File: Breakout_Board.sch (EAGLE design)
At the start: 89 parts, among them IC101 AD8620R, IC102 AD8620R, IC103 ADE7880, IC104 RH/H6, IC105 7805TV, Q101 16M384, U101 ADR512ARTZ-REEL7, U102 SI8640BD-B-IS, U103 SI8641BD-B-IS, X1 231-538/001-000, X101 STL266-04, X103 MKDSN1,5/2-5,08

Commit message: Board layout updated
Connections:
- net IAN: now also C2.2, R1.2, R3.2, X1.P2; no longer C109.2, R106.1, R112.2, X1.P8
- net IAP: now also C2.1, R2.2; no longer C109.1, R127.2
- net IBN: now also C107.2, R104.2, R110.2, X1.P3; no longer C108.2, R105.1, R111.2, X1.P6
- net IBP: now also C107.1, R125.2; no longer C108.1, R126.2
- net ICN: now also C108.2, R105.2, R111.2, X1.P6; no longer C107.2, R104.1, R110.2, X1.P4
- net ICP: now also C108.1, R126.2; no longer C107.1, R125.2
- net INN: now also C109.2, R106.1, R112.2, X1.P7; no longer C2.2, R1.1, R3.2, X1.P2
- net INP: now also C109.1, R127.2; no longer C2.1, R2.2
- net IN_I1: now also IC102A.IN+, R104.1, X1.P4; no longer IC101A.IN+, R104.2, X1.P3
- net IN_I2: now also R105.1; no longer R105.2
- net IN_I3: now also IC101A.IN+, X1.P8; no longer IC102A.IN+, X1.P7
- net N$18: now also IC101A.OUT; no longer IC102A.OUT
- net N$19: now also IC102A.IN-; no longer IC101A.IN-
- net N$21: now also IC102A.OUT; no longer IC101A.OUT
- net N$23: now also R1.1; no longer R1.2
- net N$29: now also IC101A.IN-; no longer IC102A.IN-
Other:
- moved on the sheet: IC101A, IC102A, R1, R104, R105

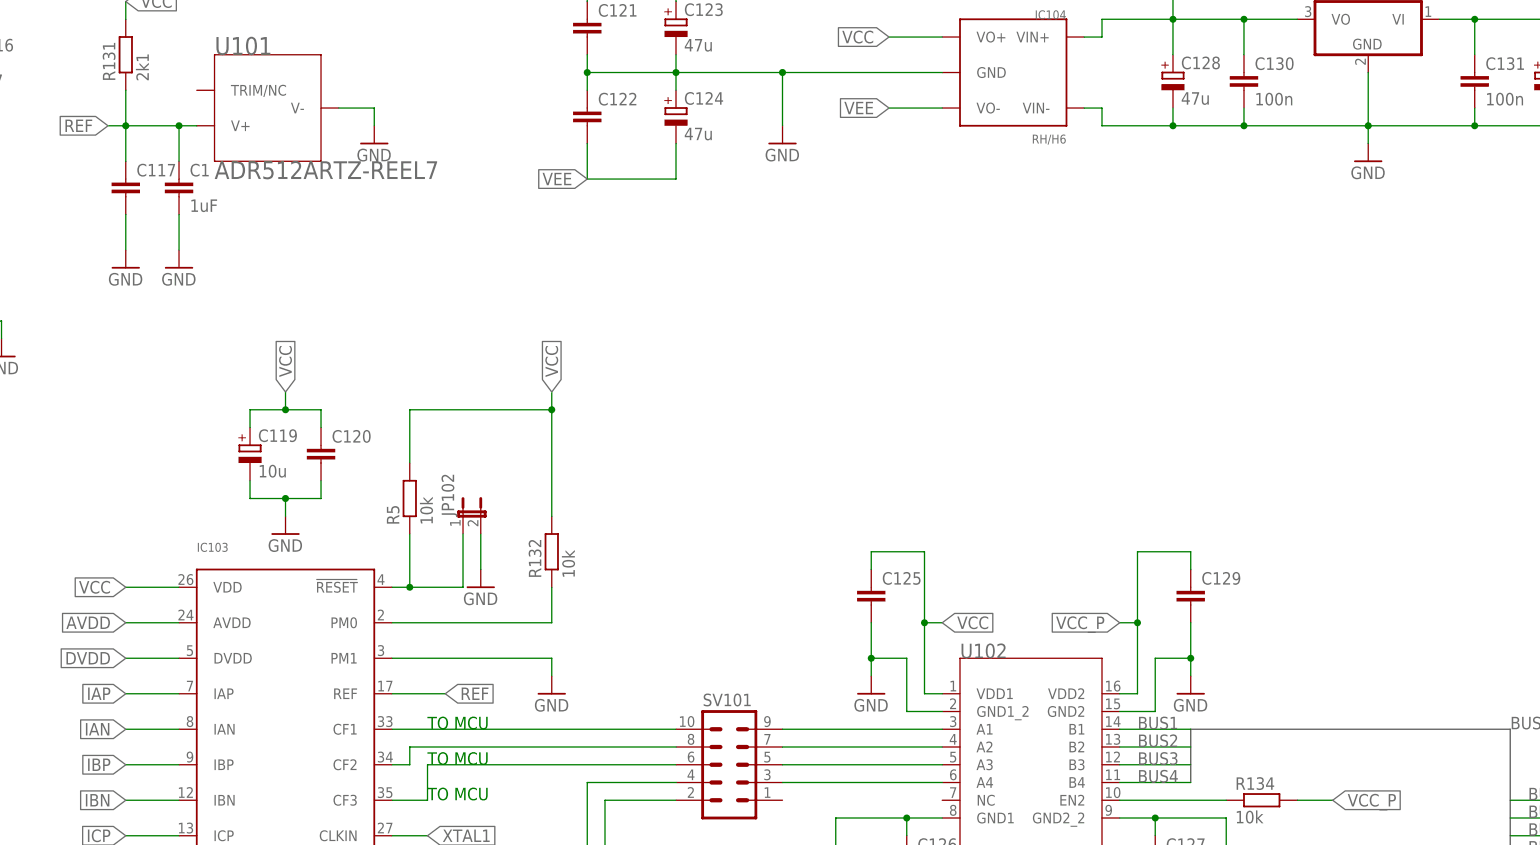
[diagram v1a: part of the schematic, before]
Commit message: Board layout finished without checking DRC
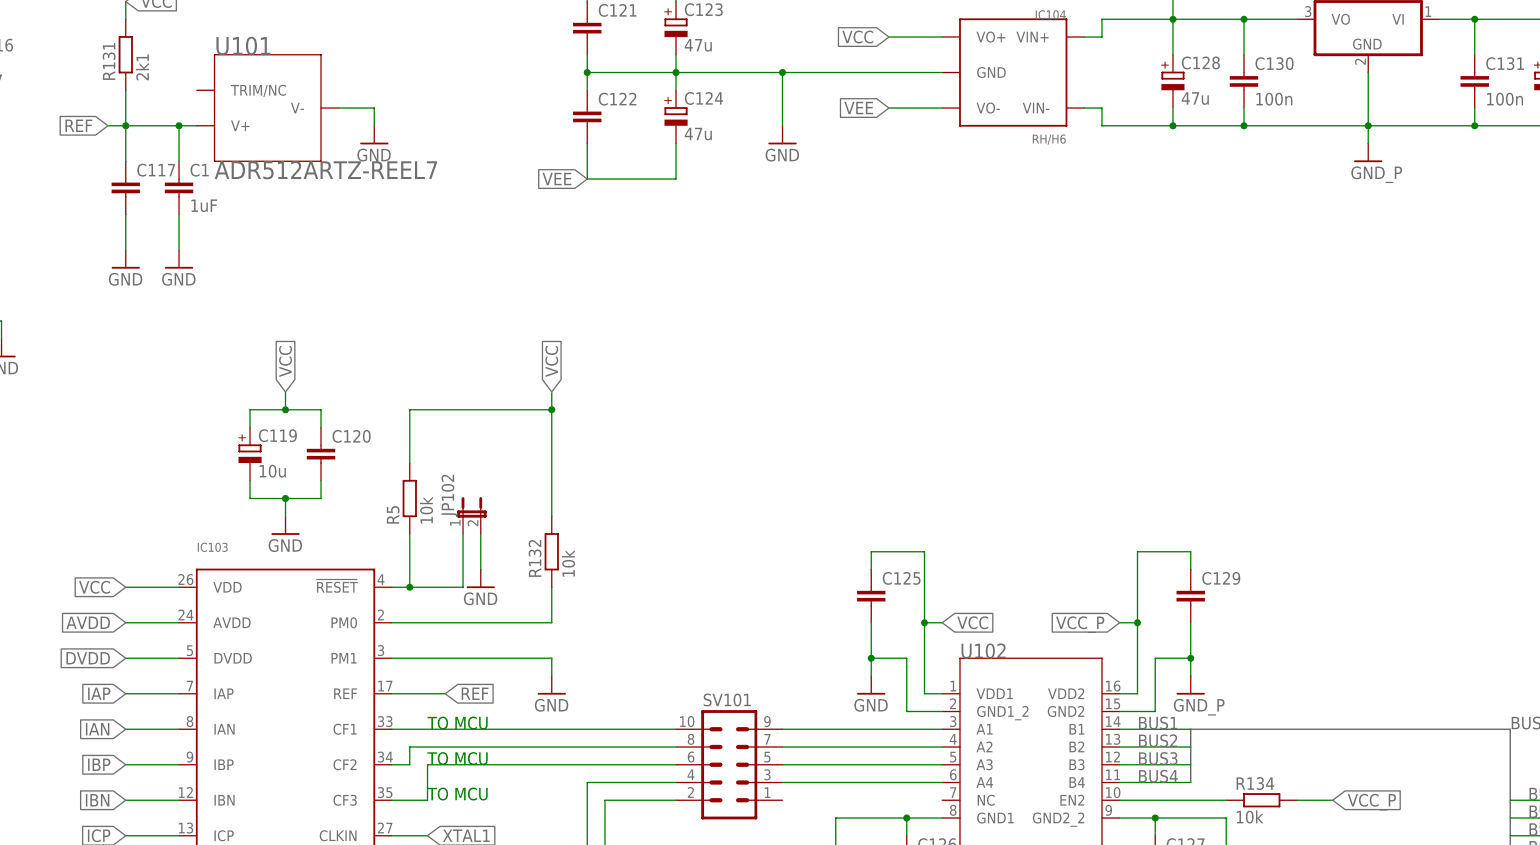
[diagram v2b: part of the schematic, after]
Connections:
- net GND: now also C117.2
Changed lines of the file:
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@@
 <part name="C127" library="rcl" deviceset="C-EU" device="C0603K" value="100n"/>
 <part name="GND115" library="supply1" deviceset="GND" device=""/>
-<part name="GND116" library="supply1" deviceset="GND" device=""/>
+<part name="GND116" library="supply1" deviceset="GND" device="" value="GND_P"/>
 <part name="GND114" library="supply1" deviceset="GND" device=""/>
 <part name="GND113" library="supply1" deviceset="GND" device=""/>
@@
 <part name="C131" library="rcl" deviceset="C-EU" device="C0603K" value="100n"/>
 <part name="C132" library="rcl" deviceset="CPOL-EU" device="D" value="47u"/>
-<part name="GND119" library="supply1" deviceset="GND" device=""/>
+<part name="GND119" library="supply1" deviceset="GND" device="" value="GND_P"/>
 <part name="SV102" library="con-lstb" deviceset="MA08-1" device=""/>
 <part name="X103" library="con-phoenix-508" deviceset="MKDSN1,5/2-5,08" device=""/>
@@
 </segment>
 </net>
-<net name="ICP" class="2">
+<net name="ICP" class="0">
 <segment>
 <pinref part="IC103" gate="G$1" pin="ICP"/>
@@
 </segment>
 <segment>
-<wire x1="165.1" y1="226.06" x2="165.1" y2="220.98" width="0.1524" layer="91"/>
-<pinref part="GND103" gate="1" pin="GND"/>
-</segment>
-<segment>
 <wire x1="172.72" y1="226.06" x2="172.72" y2="220.98" width="0.1524" layer="91"/>
 <pinref part="GND105" gate="1" pin="GND"/>
@@
 </segment>
 <segment>
-<pinref part="GND119" gate="1" pin="GND"/>
-<wire x1="342.9" y1="236.22" x2="342.9" y2="238.76" width="0.1524" layer="91"/>
-</segment>
-<segment>
 <pinref part="IC103" gate="G$1" pin="AGND"/>
 <wire x1="172.72" y1="96.52" x2="167.64" y2="96.52" width="0.1524" layer="91"/>
@@
 <wire x1="147.32" y1="210.82" x2="139.7" y2="210.82" width="0.1524" layer="91"/>
 <junction x="139.7" y="210.82"/>
+</segment>
+<segment>
+<pinref part="GND103" gate="1" pin="GND"/>
+<pinref part="C117" gate="G$1" pin="2"/>
+<wire x1="165.1" y1="220.98" x2="165.1" y2="226.06" width="0.1524" layer="91"/>
 </segment>
 </net>
@@
 <wire x1="378.46" y1="238.76" x2="368.3" y2="238.76" width="0.1524" layer="91"/>
 <junction x="368.3" y="238.76"/>
+<pinref part="GND119" gate="1" pin="GND"/>
+<wire x1="342.9" y1="238.76" x2="342.9" y2="236.22" width="0.1524" layer="91"/>
 </segment>
 </net>
@@
 </sheet>
 </sheets>
+<errors>
+</errors>
 </schematic>
 </drawing>

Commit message: First official release!
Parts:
- R1, R104, R105, R106: value 0R01 -> 4R7
- R110, R111, R112, R3: value 150R -> 6k49
- R119, R120, R121, R4: value 221k -> 2k21
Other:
- note added: "Dimensioniert auf 25 A Verstärkungsfaktor 1+ 0,3251"
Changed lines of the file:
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@@
 </class>
 <class number="1" name="HighU" width="0" drill="0">
-<clearance class="0" value="2"/>
+<clearance class="0" value="0.0254"/>
 </class>
 <class number="2" name="HIghI" width="0" drill="0">
-<clearance class="0" value="2"/>
+<clearance class="0" value="0.0254"/>
 <clearance class="1" value="2"/>
 </class>
@@
 <part name="R130" library="rcl" deviceset="R-EU_" device="R0603" value="1k"/>
 <part name="C112" library="rcl" deviceset="C-EU" device="C0603K" value="2n2"/>
-<part name="R104" library="rcl" deviceset="R-EU_" device="R0603" value="0R01"/>
+<part name="R104" library="rcl" deviceset="R-EU_" device="R0603" value="4R7"/>
 <part name="IC101" library="analog-devices" deviceset="AD8620" device="R"/>
 <part name="IC102" library="analog-devices" deviceset="AD8620" device="R"/>
 <part name="R125" library="rcl" deviceset="R-EU_" device="R0603" value="1k"/>
 <part name="C107" library="rcl" deviceset="C-EU" device="C0603K" value="2n2"/>
-<part name="R110" library="rcl" deviceset="R-EU_" device="R0603" value="150R"/>
-<part name="R119" library="rcl" deviceset="R-EU_" device="R0603" value="221k"/>
-<part name="R105" library="rcl" deviceset="R-EU_" device="R0603" value="0R01"/>
+<part name="R110" library="rcl" deviceset="R-EU_" device="R0603" value="6k49"/>
+<part name="R119" library="rcl" deviceset="R-EU_" device="R0603" value="2k21"/>
+<part name="R105" library="rcl" deviceset="R-EU_" device="R0603" value="4R7"/>
 <part name="R126" library="rcl" deviceset="R-EU_" device="R0603" value="1k"/>
 <part name="C108" library="rcl" deviceset="C-EU" device="C0603K" value="2n2"/>
-<part name="R111" library="rcl" deviceset="R-EU_" device="R0603" value="150R"/>
-<part name="R120" library="rcl" deviceset="R-EU_" device="R0603" value="221k"/>
-<part name="R106" library="rcl" deviceset="R-EU_" device="R0603" value="0R01"/>
+<part name="R111" library="rcl" deviceset="R-EU_" device="R0603" value="6k49"/>
+<part name="R120" library="rcl" deviceset="R-EU_" device="R0603" value="2k21"/>
+<part name="R106" library="rcl" deviceset="R-EU_" device="R0603" value="4R7"/>
 <part name="R127" library="rcl" deviceset="R-EU_" device="R0603" value="1k"/>
 <part name="C109" library="rcl" deviceset="C-EU" device="C0603K" value="2n2"/>
-<part name="R112" library="rcl" deviceset="R-EU_" device="R0603" value="150R"/>
-<part name="R121" library="rcl" deviceset="R-EU_" device="R0603" value="221k"/>
+<part name="R112" library="rcl" deviceset="R-EU_" device="R0603" value="6k49"/>
+<part name="R121" library="rcl" deviceset="R-EU_" device="R0603" value="2k21"/>
 <part name="IC104" library="recom_own" deviceset="RH/H6" device=""/>
 <part name="R132" library="rcl" deviceset="R-EU_" device="R0603" value="10k"/>
@@
 <part name="GND107" library="supply1" deviceset="GND" device=""/>
 <part name="C1" library="rcl" deviceset="C-EU" device="C0603K" value="1uF"/>
-<part name="R1" library="rcl" deviceset="R-EU_" device="R0603" value="0R01"/>
+<part name="R1" library="rcl" deviceset="R-EU_" device="R0603" value="4R7"/>
 <part name="R2" library="rcl" deviceset="R-EU_" device="R0603" value="1k"/>
 <part name="C2" library="rcl" deviceset="C-EU" device="C0603K" value="2n2"/>
-<part name="R3" library="rcl" deviceset="R-EU_" device="R0603" value="150R"/>
-<part name="R4" library="rcl" deviceset="R-EU_" device="R0603" value="221k"/>
+<part name="R3" library="rcl" deviceset="R-EU_" device="R0603" value="6k49"/>
+<part name="R4" library="rcl" deviceset="R-EU_" device="R0603" value="2k21"/>
 <part name="X1" library="con-wago_5.08mm" deviceset="231-538/001-000" device=""/>
 <part name="R5" library="rcl" deviceset="R-EU_" device="R0603" value="10k"/>
@@
 <text x="43.18" y="220.98" size="1.778" layer="91">29pF = 2x18pF (C_L) - 7pF (C_P)</text>
 <text x="60.96" y="218.44" size="1.778" layer="91">30pF should fit</text>
+<text x="30.48" y="198.12" size="1.778" layer="91">Dimensioniert auf 25 A
+Verstärkungsfaktor 1+ 0,3251</text>
 </plain>
 <instances>
@@
 </schematic>
 </drawing>
+<compatibility>
+<note version="6.3" minversion="6.2.2" severity="warning">
+Since Version 6.2.2 text objects can contain more than one line,
+which will not be processed correctly with this version.
+</note>
+</compatibility>
 </eagle>

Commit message: A1 schematic and layout
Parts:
- removed C102, C103, C105, C106: 220n, rcl:C-EUC0603K
- removed C107, C108, C109: 2n2, rcl:C-EUC0603K
- removed C122: (no value), rcl:C-EUC0603K
- removed C124: 47u, rcl:CPOL-EUD
- removed IC101, IC102: AD8620R, analog-devices:AD8620R
- removed IC104: RH/H6, recom_own:RH/H6
- removed R104, R105, R106: 4R7, rcl:R-EU_R0603
- removed R110, R111, R112: 6k49, rcl:R-EU_R0603
- removed R119, R120, R121: 2k21, rcl:R-EU_R0603
- removed R125, R126, R127: 1k, rcl:R-EU_R0603
- added C3, C4, C5, C6, C7, C8, C9: 2n2, rcl:C-EUC0603K
- added IC1: RH-0505S/H6, recom_own:RH-0505S/H6
- added R10, R11, R14, R15, R18, R6, R7: 2R7, rcl:R-EU_R0805
- added R12, R13, R16, R17, R8, R9: 150R, rcl:R-EU_R0805
- added R19, R20, R21, R22, R23, R24, R25: 1k, rcl:R-EU_R0603
- R1: value 4R7 -> 2R7; device rcl:R-EU_R0603 -> rcl:R-EU_R0805
- R3: value 6k49 -> 150R; device rcl:R-EU_R0603 -> rcl:R-EU_R0805
- R4: value 2k21 -> 150R; device rcl:R-EU_R0603 -> rcl:R-EU_R0805
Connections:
- removed net AGND: C113.2, C114.-
- removed net DGND: C115.2, C116.-
- removed net IN_I1: IC102A.IN+, R104.1, X1.P4
- removed net IN_I2: IC101B.IN+, R105.1, X1.P5
- removed net IN_I3: IC101A.IN+, R106.2, X1.P8
- removed net N$16: IC101B.OUT, R120.1, R126.1
- removed net N$17: IC102B.IN-, R3.1, R4.2
- removed net N$18: IC101A.OUT, R121.1, R127.1
- removed net N$19: IC102A.IN-, R110.1, R119.2
- removed net N$21: IC102A.OUT, R119.1, R125.1
- removed net N$22: IC102B.OUT, R2.1, R4.1
- removed net N$23: IC102B.IN+, R1.1, X1.P1
- removed net N$24: IC101B.IN-, R111.1, R120.2
- removed net N$29: IC101A.IN-, R112.1, R121.2
- removed net VEE: C103.2, C106.2, C122.2, C124.-, IC101P.V-, IC102P.V-, IC104.VO-
- new net INH: R15.2, R16.2, R24.1, X1.P7
- new net INL: R17.1, R18.1, R25.1, X1.P8
- new net L1H: R1.2, R2.1, R3.2, X1.P1
- new net L1L: R19.1, R4.1, R6.1, X1.P2
- new net L2H: R20.1, R7.2, R8.2, X1.P3
- new net L2L: R10.1, R21.1, R9.1, X1.P4
- new net L3H: R11.2, R12.2, R22.1, X1.P5
- new net L3L: R13.1, R14.1, R23.1, X1.P6
- net GND: now also C113.2, C114.-, C115.2, C116.-, C2.2, C3.1, C4.2, C5.1, C6.2, C7.1, C8.2, C9.1, IC1.VOUT-, R1.1, R10.2, R11.1, R12.1, R13.2, R14.2, R15.1, R16.1, R17.2, R18.2, R3.1, R4.2, R6.2, R7.1, R8.1, R9.2; no longer C102.2, C103.1, C105.2, C106.1, C122.1, C124.+, IC104.GND
- net GND_P: now also IC1.VIN-; no longer IC104.VIN-
- net IAN: now also C3.2, R19.2; no longer C2.2, R1.2, R3.2, X1.P2
- net IBN: now also C5.2, R21.2; no longer C107.2, R104.2, R110.2, X1.P3
- net IBP: now also C4.1, R20.2; no longer C107.1, R125.2
- net ICN: now also C7.2, R23.2; no longer C108.2, R105.2, R111.2, X1.P6
- net ICP: now also C6.1, R22.2; no longer C108.1, R126.2
- net INN: now also C9.2, R25.2; no longer C109.2, R106.1, R112.2, X1.P7
- net INP: now also C8.1, R24.2; no longer C109.1, R127.2
- net VCC: now also IC1.VOUT+; no longer C102.1, C105.1, IC101P.V+, IC102P.V+, IC104.VO+
- net VCC_P: now also IC1.VIN+; no longer IC104.VIN+
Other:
- note removed: "29pF = 2x18pF (C_L) - 7pF (C_P)"
- note removed: "30pF should fit"
- note removed: "Dimensioniert auf 25 A Verstärkungsfaktor 1+ 0,3251"
- moved on the sheet: C121, C123, C2, R1, R2, R3, R4, X1

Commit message: -updated sch and brd, added pdf files
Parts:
- removed C1: 1uF, rcl:C-EUC0603K
- removed C132: 47u, rcl:CPOL-EUD
- removed C2, C5: 2n2, rcl:C-EUC0603K
- removed IC105: 7805TV, linear:7805TV
- removed R1, R15, R18, R6, R7: 2R7, rcl:R-EU_R0805
- removed R17, R3, R4, R8, R9: 150R, rcl:R-EU_R0805
- removed R20, R21, R22, R23, R24, R25: 1k, rcl:R-EU_R0603
- removed R5: 10k, rcl:R-EU_R0603
- removed X1: 231-538/001-000, con-wago_5.08mm:231-538/001-000
- added C109: 2n2, rcl:C-EUC0603K
- added C118: 10u, rcl:CPOL-EUB
- added C122, C124: 100n, rcl:C-EUC0603K
- added IC101: ADE7880, AnalogDevices_own:ADE7880
- added R104, R105, R106: 162k, rcl:R-EU_R0805
- added R125, R136: 196k, rcl:R-EU_R0805
- added R137, R138, R139: 1k, rcl:R-EU_R0805
- added R140, R141, R142: 1k, rcl:R-EU_R0603
- added R143: 2k1, rcl:R-EU_R0603
- added R144, R145, R146, R147, R148, R149, R150, R151, R152: 10k, rcl:R-EU_R0603
- added X102: STL266-04, con-riacon:STL266-04
- C101, C104: value 30pF -> 2n2
- C112: value 2n2 -> 220n
- C113: value 220n -> 4u7; device rcl:C-EUC0603K -> rcl:CPOL-EUB
- C114, C116: value 4u7 -> 30pF; device rcl:CPOL-EUB -> rcl:C-EUC0603K
- C117: value (none) -> 4u7; device rcl:C-EUC0603K -> rcl:CPOL-EUB
- C119: value 10u -> 100n; device rcl:CPOL-EUB -> rcl:C-EUC0603K
- C120, C125, C129: value (none) -> 100n
- C121: value (none) -> 1uF
- C127, C131: value 100n -> 47u; device rcl:C-EUC0603K -> rcl:CPOL-EUD
- C128: value 47u -> 100n; device rcl:CPOL-EUD -> rcl:C-EUC0603K
- IC103: value ADE7880 -> 7805TV; device AnalogDevices_own:ADE7880 -> linear:7805TV
- R107, R108, R109: value 162k -> 2R7
- R113, R114: value 196k -> 2R7
- R115, R116, R117, R118: value 196k -> 150R
- R122: value 1k -> 150R
- R123, R124: value 1k -> 196k
- R131: value 2k1 -> 1k
- R132, R133: value 10k -> 1k
- R134, R135: value 10k -> 196k; device rcl:R-EU_R0603 -> rcl:R-EU_R0805
- X101: value STL266-04 -> 231-538/001-000; device con-riacon:STL266-04 -> con-wago_5.08mm:231-538/001-000
- renumbered C3 to C102, C4 to C103, C6 to C105, C7 to C106, C8 to C107, C9 to C108, IC1 to IC102, R10 to R110, R11 to R111, R12 to R119, R13 to R120, R14 to R112, R16 to R121, R19 to R127, R2 to R126
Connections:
- removed net N$42: R133.2, U103.EN2
- new net N$16: R150.2, U103.EN2
- net !SS: now also IC101.!SS, R149.1; no longer IC103.!SS
- net AVDD: now also C112.1, C113.+, IC101.AVDD; no longer C113.1, C114.+, IC103.AVDD
- net DVDD: now also C117.+, IC101.DVDD; no longer C116.+, IC103.DVDD
- net GND: now also C112.2, C113.-, C114.2, C116.1, C117.-, C118.-, C119.2, C122.2, C124.2, C125.1, IC101.AGND, IC101.DGND, IC101.PM1, R107.1, R108.2, R109.1, R113.1, R114.2, R115.1, R116.2, R117.1, R118.2, R122.2; no longer C1.2, C113.2, C114.-, C116.-, C117.2, C119.-, C125.2, C126.1, C2.2, C5.1, IC103.AGND, IC103.DGND, IC103.PM1, R1.1, R15.1, R17.2, R18.2, R3.1, R4.2, R6.2, R7.1, R8.1, R9.2
- net GND_P: now also C126.1, C127.-, C128.2, C131.-, IC103.GND; no longer C127.1, C128.-, C131.2, C132.-, IC105.GND
- net IAN: now also IC101.IAN; no longer IC103.IAN
- net IAP: now also C101.1, IC101.IAP; no longer C2.1, IC103.IAP
- net IBN: now also C104.2, IC101.IBN, R129.2; no longer C5.2, IC103.IBN, R21.2
- net IBP: now also IC101.IBP, R128.2; no longer IC103.IBP, R20.2
- net ICN: now also IC101.ICN, R131.2; no longer IC103.ICN, R23.2
- net ICP: now also IC101.ICP, R130.2; no longer IC103.ICP, R22.2
- net INH: now also R113.2, R132.1, X101.P7; no longer R15.2, R24.1, X1.P7
- net INL: now also R114.1, R122.1, R133.1, X101.P8; no longer R17.1, R18.1, R25.1, X1.P8
- net INN: now also IC101.INN, R133.2; no longer IC103.INN, R25.2
- net INP: now also IC101.INP, R132.2; no longer IC103.INP, R24.2
- net L1H: now also R107.2, R115.2, X101.P1; no longer R1.2, R3.2, X1.P1
- net L1L: now also R108.1, R116.1, X101.P2; no longer R4.1, R6.1, X1.P2
- net L2H: now also R109.2, R117.2, R128.1, X101.P3; no longer R20.1, R7.2, R8.2, X1.P3
- net L2L: now also R118.1, R129.1, X101.P4; no longer R21.1, R9.1, X1.P4
- net L3H: now also R130.1, X101.P5; no longer R22.1, X1.P5
- net L3L: now also R131.1, X101.P6; no longer R23.1, X1.P6
- net MISO: now also IC101.MISO, R147.1; no longer IC103.MISO
- net MOSI: now also IC101.MOSI, R148.1; no longer IC103.MOSI
- net N$1: now also R104.1; no longer R107.1
- net N$10: now also X102.3; no longer X101.3
- net N$11: now also R106.1; no longer R109.1
- net N$12: now also R106.2, R125.1; no longer R109.2, R115.1
- net N$13: now also R125.2, R136.1; no longer R115.2, R118.1
- net N$14: now also R136.2, R139.2, R142.1; no longer R118.2, R124.2, R130.1
- net N$15: now also X102.2; no longer X101.2
- net N$2: now also R104.2, R123.1; no longer R107.2, R113.1
- net N$25: now also IC101.PM0, R145.1; no longer IC103.PM0, R132.1
- net N$3: now also R123.2, R134.1; no longer R113.2, R116.1
- net N$30: now also IC101.!RESET, R144.1; no longer IC103.!RESET, R5.1
- net N$35: now also IC101.CF1; no longer IC103.CF1
- net N$36: now also IC101.CF2; no longer IC103.CF2
- net N$37: now also IC101.CF3; no longer IC103.CF3
- net N$38: now also IC101.!IRQ0; no longer IC103.!IRQ0
- net N$39: now also IC101.!IRQ1; no longer IC103.!IRQ1
- net N$4: now also R134.2, R137.2, R140.1; no longer R116.2, R122.2, R128.1
- net N$40: now also R152.1; no longer R135.1
- net N$41: now also R151.1; no longer R134.1
- net N$46: now also C130.1, C131.+, IC103.VI; no longer C131.1, C132.+, IC105.VI
- net N$5: now also X102.4; no longer X101.4
- net N$6: now also R105.1; no longer R108.1
- net N$7: now also R105.2, R124.1; no longer R108.2, R114.1
- net N$8: now also R124.2, R135.1; no longer R114.2, R117.1
- net N$9: now also R135.2, R138.2, R141.1; no longer R117.2, R123.2, R129.1
- net REF: now also C119.1, C121.1, IC101.REF, R143.1; no longer C1.1, C117.1, IC103.REF, R131.1
- net SCLK: now also IC101.SCLK, R146.1; no longer IC103.SCLK
- net VAP: now also C109.1, IC101.VAP, R140.2; no longer C110.1, IC103.VAP, R128.2
- net VBP: now also C110.1, IC101.VBP, R141.2; no longer C111.1, IC103.VBP, R129.2
- net VCC: now also C118.+, C122.1, C124.1, C125.2, IC101.VDD, R143.2, R144.2, R145.2, R146.2, R147.2, R148.2, R149.2, R150.1; no longer C119.+, C121.1, C125.1, C126.2, IC103.VDD, R131.2, R132.2, R133.1, R5.2
- net VCC_P: now also C126.2, C127.+, C128.1, IC103.VO, R151.2, R152.2; no longer C127.2, C128.+, C130.1, IC105.VO, R134.2, R135.2
- net VCP: now also C111.1, IC101.VCP, R142.2; no longer C112.1, IC103.VCP, R130.2
- net VN: now also C109.2, IC101.VN, R137.1, R138.1, R139.1, X102.1; no longer C112.2, IC103.VN, R122.1, R123.1, R124.1, X101.1
- net XTAL1: now also C116.2, IC101.CLKIN; no longer C104.2, IC103.CLKIN
- net XTAL2: now also C114.1, IC101.CLKOUT; no longer C101.1, IC103.CLKOUT
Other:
- moved on the sheet: C101, C104, C110, C111, C112, C120, C121, C125, C126, C129, C130, JP101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
